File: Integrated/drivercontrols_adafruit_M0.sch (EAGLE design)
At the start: 22 parts

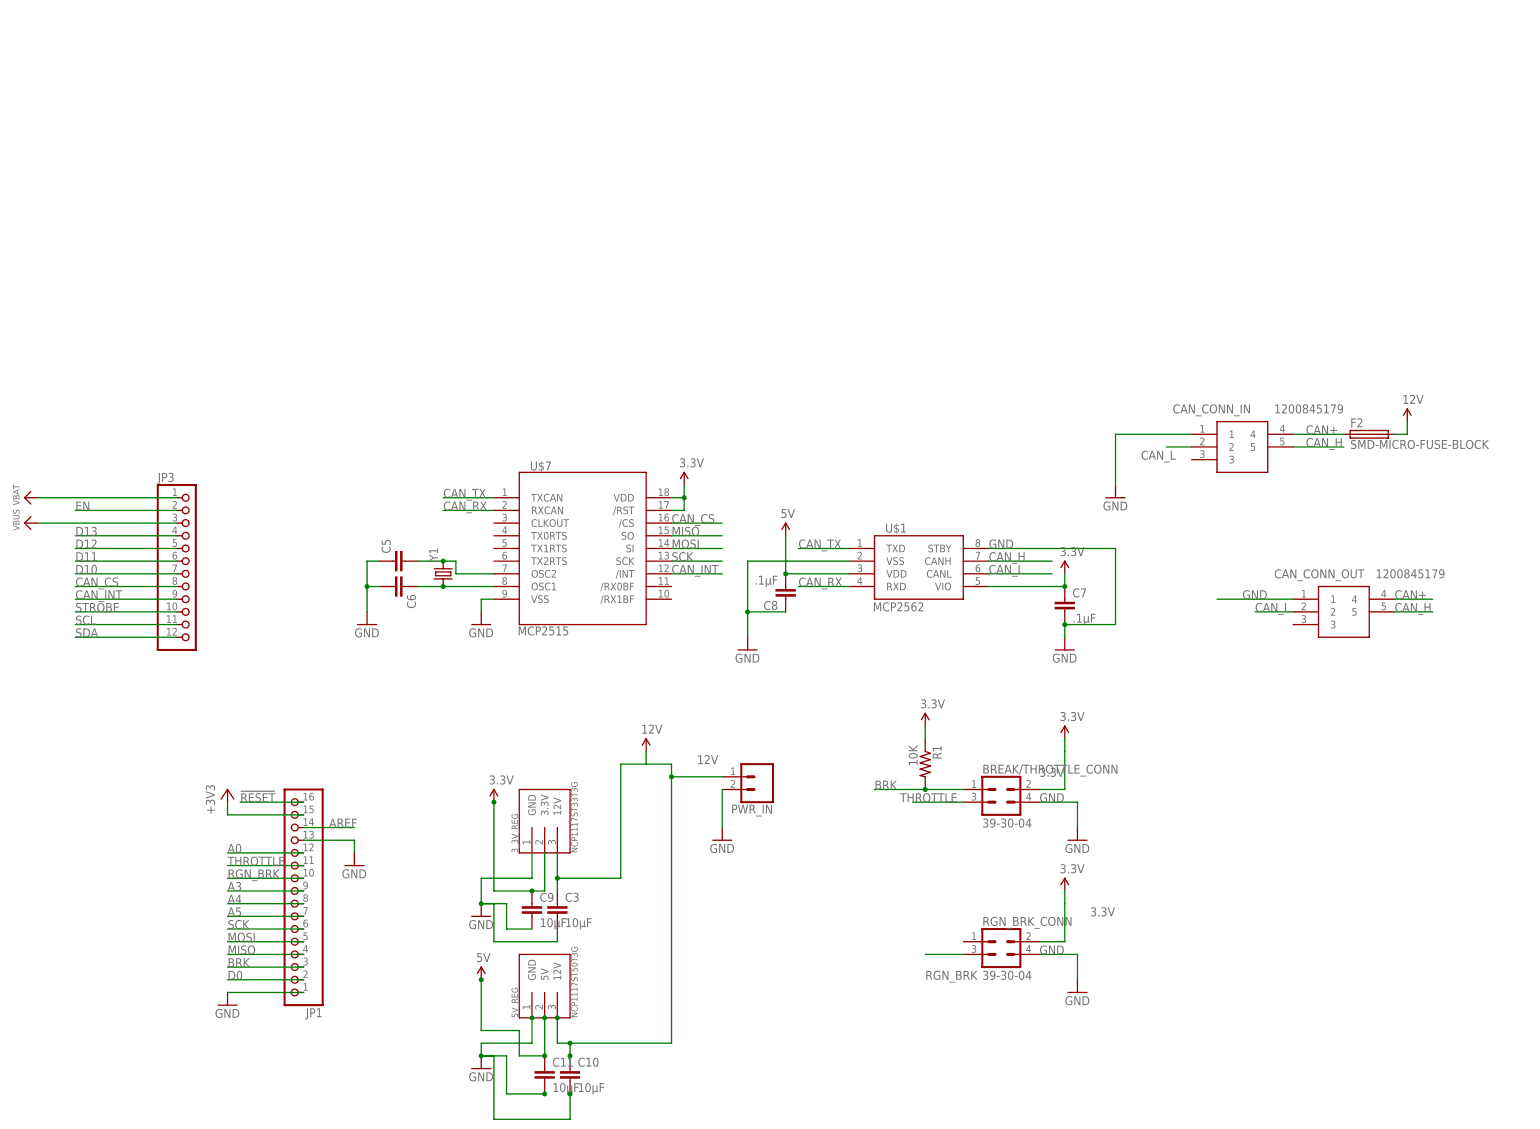
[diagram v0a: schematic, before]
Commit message: drver control side of board no DRC
DRCs fixed, 12V power coming in from CAN connectors
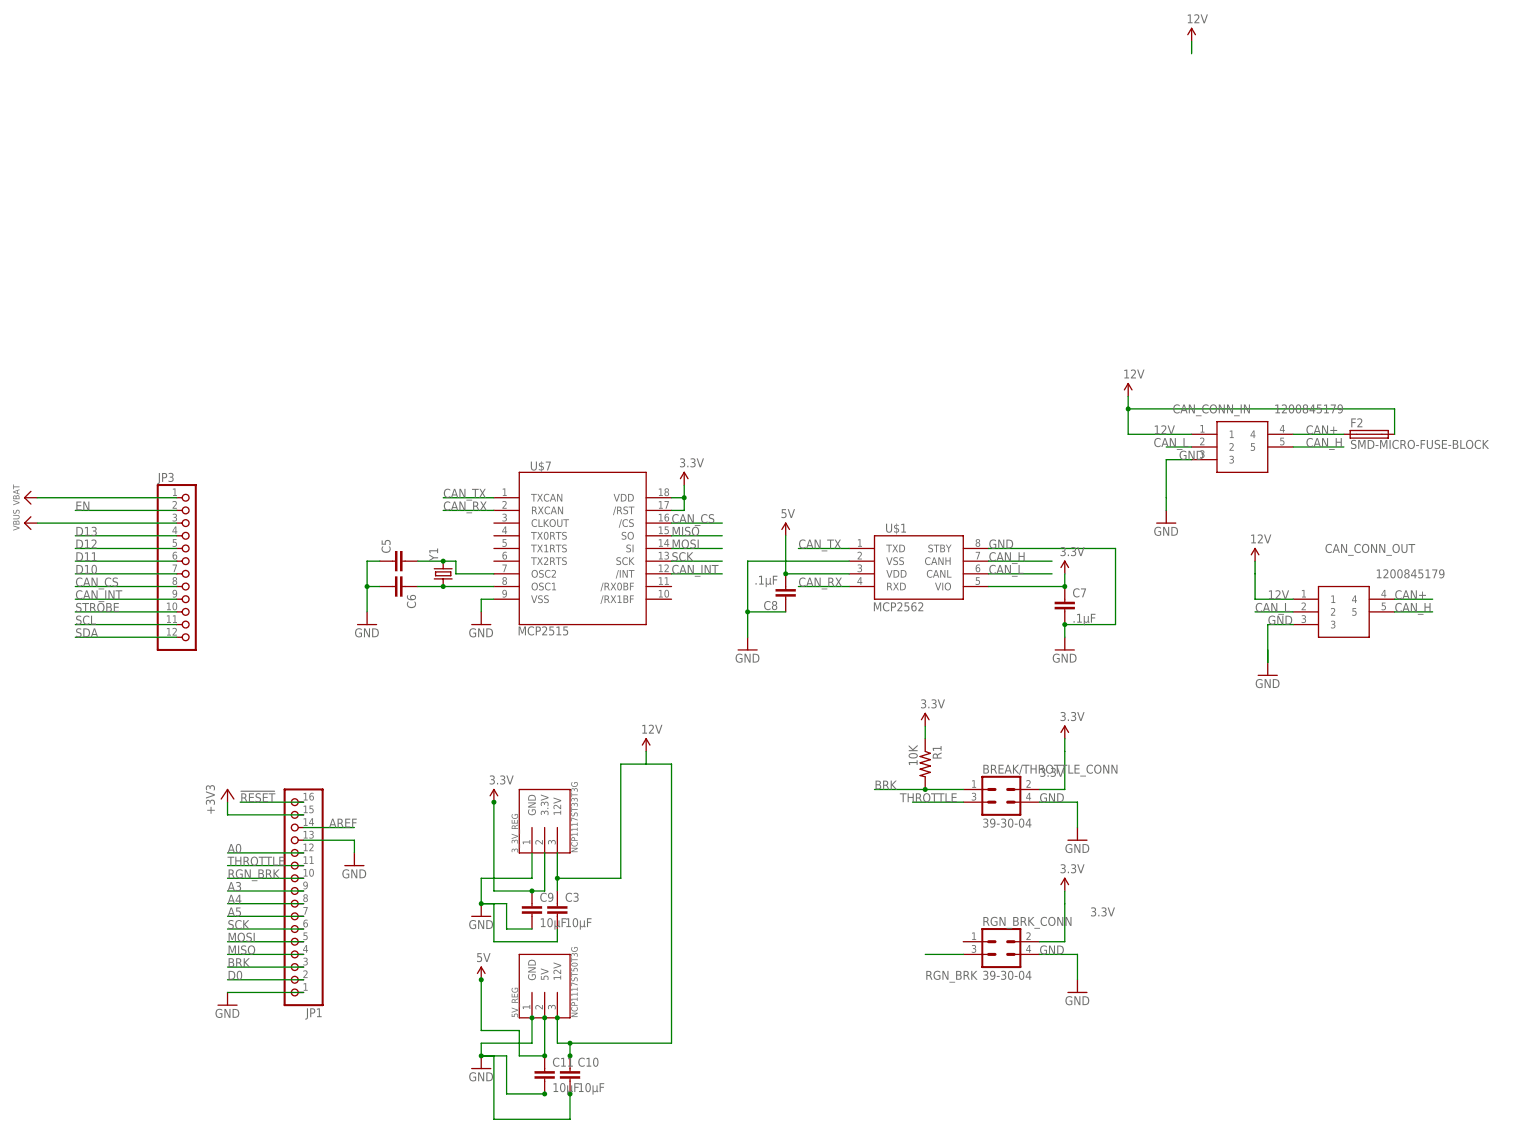
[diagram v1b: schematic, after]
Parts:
- removed PWR_IN: (no value), SparkFun-Connectors:CONN_02
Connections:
- net 12V: now also CAN_CONN_IN.1, CAN_CONN_OUT.1; no longer PWR_IN.1
- net GND: now also CAN_CONN_IN.3, CAN_CONN_OUT.3; no longer CAN_CONN_IN.1, CAN_CONN_OUT.1, PWR_IN.2
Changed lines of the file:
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@@
 <part name="U$20" library="microbuilder" deviceset="VBAT" device=""/>
 <part name="JP3" library="microbuilder" deviceset="HEADER-1X12" device=""/>
-<part name="PWR_IN" library="SparkFun-Connectors" library_urn="urn:adsk.eagle:library:513" deviceset="CONN_02" device="" package3d_urn="urn:adsk.eagle:package:38039/1"/>
-<part name="GND3" library="SparkFun-Aesthetics" deviceset="GND" device=""/>
 <part name="SUPPLY1" library="SparkFun-Aesthetics" deviceset="12V" device=""/>
 <part name="BREAK/THROTTLE_CONN" library="con-molex-mini-fit" deviceset="39-30-?04?" device=""/>
@@
 <part name="SUPPLY11" library="SparkFun-Aesthetics" deviceset="3.3V" device=""/>
 <part name="CAN_CONN_IN" library="SamacSys_Parts" deviceset="1200845179" device=""/>
+<part name="F2" library="f-lf-omniblok-s" deviceset="SMD-MICRO-FUSE" device="-BLOCK"/>
+<part name="CAN_CONN_OUT" library="SamacSys_Parts" deviceset="1200845179" device=""/>
+<part name="SUPPLY9" library="SparkFun-Aesthetics" deviceset="12V" device=""/>
+<part name="GND9" library="SparkFun-Aesthetics" deviceset="GND" device=""/>
+<part name="SUPPLY12" library="SparkFun-Aesthetics" deviceset="12V" device=""/>
+<part name="SUPPLY13" library="SparkFun-Aesthetics" deviceset="12V" device=""/>
 <part name="GND13" library="SparkFun-Aesthetics" deviceset="GND" device=""/>
-<part name="F2" library="f-lf-omniblok-s" deviceset="SMD-MICRO-FUSE" device="-BLOCK"/>
-<part name="SUPPLY10" library="SparkFun-Aesthetics" deviceset="12V" device=""/>
-<part name="CAN_CONN_OUT" library="SamacSys_Parts" deviceset="1200845179" device=""/>
 </parts>
 <sheets>
@@
 <attribute name="VALUE" x="95.25" y="86.36" size="1.778" layer="96"/>
 </instance>
-<instance part="PWR_IN" gate="G$1" x="215.9" y="63.5" smashed="yes" rot="R180">
-<attribute name="VALUE" x="218.44" y="68.326" size="1.778" layer="96" font="vector" rot="R180"/>
-<attribute name="NAME" x="218.44" y="57.912" size="1.778" layer="95" font="vector" rot="R180"/>
-</instance>
-<instance part="GND3" gate="1" x="208.28" y="50.8" smashed="yes">
-<attribute name="VALUE" x="205.74" y="48.26" size="1.778" layer="96"/>
-</instance>
 <instance part="SUPPLY1" gate="G$1" x="193.04" y="68.58" smashed="yes">
 <attribute name="VALUE" x="192.024" y="72.136" size="1.778" layer="96"/>
@@
 <attribute name="VALUE" x="318.77" y="137.16" size="1.778" layer="96" align="center-left"/>
 </instance>
-<instance part="GND13" gate="1" x="287.02" y="119.38" smashed="yes">
-<attribute name="VALUE" x="284.48" y="116.84" size="1.778" layer="96"/>
-</instance>
 <instance part="F2" gate="F1" x="337.82" y="132.08" smashed="yes">
 <attribute name="NAME" x="334.01" y="133.477" size="1.778" layer="95"/>
 <attribute name="VALUE" x="334.01" y="129.159" size="1.778" layer="96"/>
 </instance>
-<instance part="SUPPLY10" gate="G$1" x="345.44" y="134.62" smashed="yes">
-<attribute name="VALUE" x="344.424" y="138.176" size="1.778" layer="96"/>
-</instance>
 <instance part="CAN_CONN_OUT" gate="G$1" x="322.58" y="99.06" smashed="yes">
-<attribute name="NAME" x="318.77" y="104.14" size="1.778" layer="95" align="center-left"/>
+<attribute name="NAME" x="328.93" y="109.22" size="1.778" layer="95" align="center-left"/>
 <attribute name="VALUE" x="339.09" y="104.14" size="1.778" layer="96" align="center-left"/>
+</instance>
+<instance part="SUPPLY9" gate="G$1" x="289.56" y="139.7" smashed="yes">
+<attribute name="VALUE" x="288.544" y="143.256" size="1.778" layer="96"/>
+</instance>
+<instance part="GND9" gate="1" x="297.18" y="114.3" smashed="yes">
+<attribute name="VALUE" x="294.64" y="111.76" size="1.778" layer="96"/>
+</instance>
+<instance part="SUPPLY12" gate="G$1" x="302.26" y="210.82" smashed="yes">
+<attribute name="VALUE" x="301.244" y="214.376" size="1.778" layer="96"/>
+</instance>
+<instance part="SUPPLY13" gate="G$1" x="314.96" y="106.68" smashed="yes">
+<attribute name="VALUE" x="313.944" y="110.236" size="1.778" layer="96"/>
+</instance>
+<instance part="GND13" gate="1" x="317.5" y="83.82" smashed="yes">
+<attribute name="VALUE" x="314.96" y="81.28" size="1.778" layer="96"/>
 </instance>
 </instances>
@@
 <wire x1="175.26" y1="43.18" x2="175.26" y2="40.64" width="0.1524" layer="91"/>
 <wire x1="187.96" y1="66.04" x2="187.96" y2="43.18" width="0.1524" layer="91"/>
-<wire x1="198.12" y1="66.04" x2="198.12" y2="63.5" width="0.1524" layer="91"/>
-<wire x1="198.12" y1="63.5" x2="198.12" y2="10.16" width="0.1524" layer="91"/>
+<wire x1="198.12" y1="66.04" x2="198.12" y2="10.16" width="0.1524" layer="91"/>
 <wire x1="198.12" y1="10.16" x2="177.8" y2="10.16" width="0.1524" layer="91"/>
 <pinref part="5V_REG" gate="G$1" pin="12V"/>
@@
 <junction x="177.8" y="7.62"/>
 <wire x1="177.8" y1="10.16" x2="177.8" y2="7.62" width="0.1524" layer="91"/>
-<pinref part="PWR_IN" gate="G$1" pin="1"/>
-<wire x1="208.28" y1="63.5" x2="198.12" y2="63.5" width="0.1524" layer="91"/>
-<junction x="198.12" y="63.5"/>
-<label x="203.2" y="66.04" size="1.778" layer="95"/>
-</segment>
-<segment>
+</segment>
+<segment>
+<pinref part="CAN_CONN_IN" gate="G$1" pin="1"/>
+<wire x1="302.26" y1="132.08" x2="289.56" y2="132.08" width="0.1524" layer="91"/>
+<wire x1="289.56" y1="132.08" x2="289.56" y2="137.16" width="0.1524" layer="91"/>
+<label x="294.64" y="132.08" size="1.778" layer="95"/>
+<pinref part="SUPPLY9" gate="G$1" pin="12V"/>
 <pinref part="F2" gate="F1" pin="2"/>
-<pinref part="SUPPLY10" gate="G$1" pin="12V"/>
-<wire x1="342.9" y1="132.08" x2="345.44" y2="132.08" width="0.1524" layer="91"/>
-<wire x1="345.44" y1="132.08" x2="345.44" y2="134.62" width="0.1524" layer="91"/>
+<wire x1="289.56" y1="137.16" x2="289.56" y2="139.7" width="0.1524" layer="91"/>
+<wire x1="289.56" y1="137.16" x2="342.9" y2="137.16" width="0.1524" layer="91"/>
+<wire x1="342.9" y1="137.16" x2="342.9" y2="132.08" width="0.1524" layer="91"/>
+<junction x="289.56" y="137.16"/>
+</segment>
+<segment>
+<pinref part="SUPPLY12" gate="G$1" pin="12V"/>
+<wire x1="302.26" y1="208.28" x2="302.26" y2="210.82" width="0.1524" layer="91"/>
+</segment>
+<segment>
+<pinref part="SUPPLY13" gate="G$1" pin="12V"/>
+<wire x1="314.96" y1="104.14" x2="314.96" y2="106.68" width="0.1524" layer="91"/>
+<pinref part="CAN_CONN_OUT" gate="G$1" pin="1"/>
+<wire x1="322.58" y1="99.06" x2="314.96" y2="99.06" width="0.1524" layer="91"/>
+<wire x1="314.96" y1="99.06" x2="314.96" y2="104.14" width="0.1524" layer="91"/>
+<label x="317.5" y="99.06" size="1.778" layer="95"/>
 </segment>
 </net>
@@
 <wire x1="302.26" y1="129.54" x2="297.18" y2="129.54" width="0.1524" layer="91"/>
 <pinref part="CAN_CONN_IN" gate="G$1" pin="2"/>
-<label x="292.1" y="127" size="1.778" layer="95"/>
+<label x="294.64" y="129.54" size="1.778" layer="95"/>
 </segment>
 <segment>
@@
 </segment>
 <segment>
-<pinref part="PWR_IN" gate="G$1" pin="2"/>
-<wire x1="208.28" y1="60.96" x2="208.28" y2="53.34" width="0.1524" layer="91"/>
-<pinref part="GND3" gate="1" pin="GND"/>
-</segment>
-<segment>
 <pinref part="BREAK/THROTTLE_CONN" gate="G$1" pin="4"/>
 <wire x1="271.78" y1="58.42" x2="279.4" y2="58.42" width="0.1524" layer="91"/>
@@
 </segment>
 <segment>
+<pinref part="GND9" gate="1" pin="GND"/>
+<wire x1="297.18" y1="119.38" x2="297.18" y2="116.84" width="0.1524" layer="91"/>
+</segment>
+<segment>
+<pinref part="CAN_CONN_IN" gate="G$1" pin="3"/>
+<wire x1="302.26" y1="127" x2="297.18" y2="127" width="0.1524" layer="91"/>
+<wire x1="297.18" y1="127" x2="297.18" y2="119.38" width="0.1524" layer="91"/>
+<label x="299.72" y="127" size="1.778" layer="95"/>
+</segment>
+<segment>
 <pinref part="GND13" gate="1" pin="GND"/>
-<wire x1="287.02" y1="121.92" x2="287.02" y2="132.08" width="0.1524" layer="91"/>
-<pinref part="CAN_CONN_IN" gate="G$1" pin="1"/>
-<wire x1="302.26" y1="132.08" x2="287.02" y2="132.08" width="0.1524" layer="91"/>
-</segment>
-<segment>
-<pinref part="CAN_CONN_OUT" gate="G$1" pin="1"/>
-<wire x1="322.58" y1="99.06" x2="307.34" y2="99.06" width="0.1524" layer="91"/>
-<label x="312.42" y="99.06" size="1.778" layer="95"/>
-</segment>
-</net>
+<wire x1="317.5" y1="88.9" x2="317.5" y2="86.36" width="0.1524" layer="91"/>
+</segment>
+<segment>
+<pinref part="CAN_CONN_OUT" gate="G$1" pin="3"/>
+<wire x1="322.58" y1="93.98" x2="317.5" y2="93.98" width="0.1524" layer="91"/>
+<wire x1="317.5" y1="93.98" x2="317.5" y2="86.36" width="0.1524" layer="91"/>
+<label x="317.5" y="93.98" size="1.778" layer="95"/>
+</segment>
+</net>
